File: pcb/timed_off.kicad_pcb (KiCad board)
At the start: 2 copper layers, 19 parts, among them J1 L, J2 N, J3 L, J4 N, U1 ATtiny10-TS, U2 SPA4191

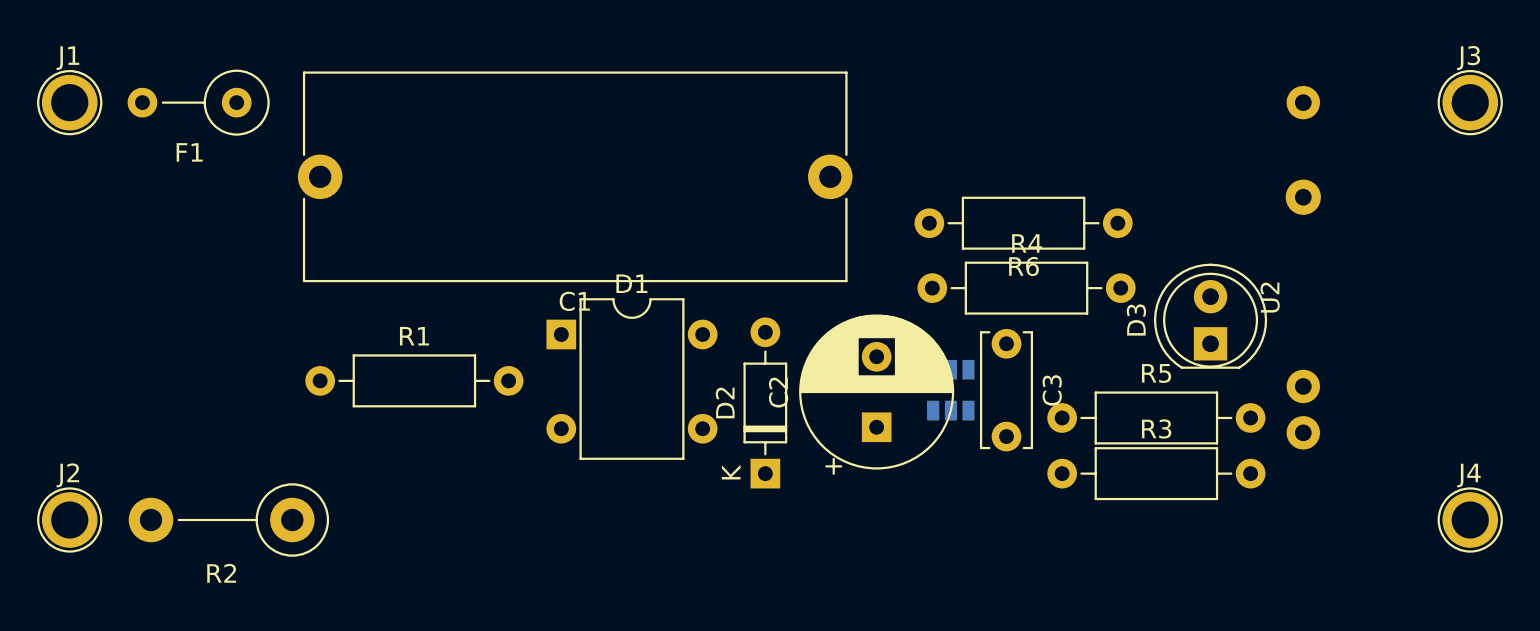
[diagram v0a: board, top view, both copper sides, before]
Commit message: fix bridge footprint, add second dropper cap footprint
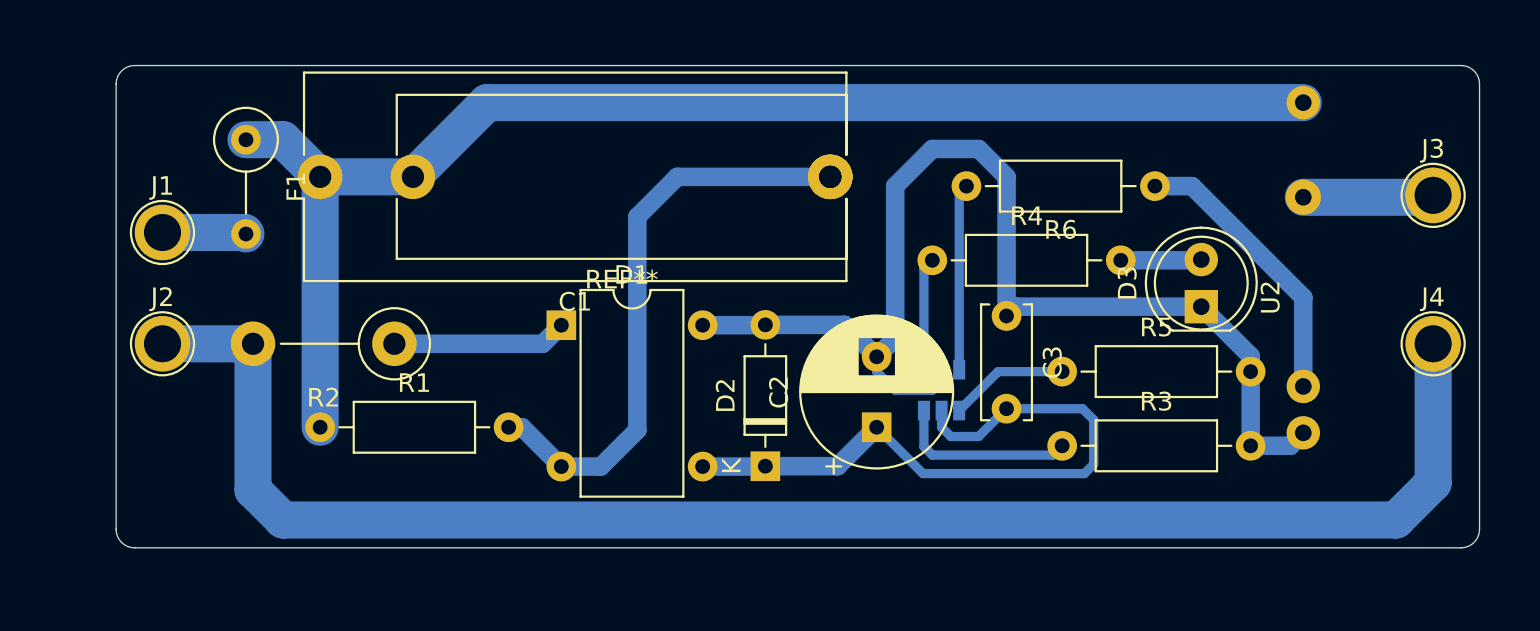
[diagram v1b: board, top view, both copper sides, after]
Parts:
- added REF**: C_Rect_L24.0mm_W8.6mm_P22.50mm_MKT, Capacitor_THT:C_Rect_L24.0mm_W8.6mm_P22.50mm_MKT, F.Cu at (120.5, 78.5)
- D1: footprint Diode_THT:Diode_Bridge_DIP-4_W7.62mm_P5.08mm -> pl_Rectifier:S1WB
- moved R2 11.0 mm to (97.0, 87.5)
- moved J2 10.7 mm to (84.5, 87.5)
- moved J4 9.71 mm to (153.0, 87.5)
- moved J1 8.60 mm to (84.5, 81.5)
- moved J3 5.39 mm to (153.0, 79.5)
- moved R6 2.83 mm to (138.0, 79.0)
- moved R1 2.50 mm to (93.0, 92.0)
- moved R5 2.50 mm to (133.0, 89.0)
- moved D3 2.06 mm to (140.5, 85.5)
- moved F1 2.06 mm to (89.0, 76.5), turned to 270 degrees
- moved C3 1.50 mm to (130.0, 86.0)
- moved R3 1.50 mm to (133.0, 93.0)
- moved R4 1.50 mm to (126.0, 83.0)
- moved D1 0.50 mm to (106.0, 86.5)
- moved U1 0.50 mm to (126.5, 90.0)
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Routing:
- net /N: track 0.00 -> 85.4 mm
- net /L: track 0.00 -> 73.0 mm
- net GND: track 0.00 -> 62.6 mm
- net Net-(C2-Pad1): track 0.00 -> 35.8 mm
- net Net-(C1-Pad1): track 0.00 -> 31.4 mm
- net Net-(R6-Pad1): track 0.00 -> 15.3 mm
- net Net-(R6-Pad2): track 0.00 -> 10.1 mm
- net Net-(R3-Pad1): track 0.00 -> 9.79 mm
- net Net-(D1-Pad1): track 0.00 -> 9.41 mm
- net Net-(J3-Pad1): track 0.00 -> 7.04 mm
- net Net-(R5-Pad1): track 0.00 -> 6.42 mm
- net Net-(R4-Pad1): track 0.00 -> 6.09 mm
- net Net-(F1-Pad2): track 0.00 -> 4.53 mm
- net Net-(D3-Pad2): track 0.00 -> 4.36 mm
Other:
- board outline added: 73.5 x 26 mm
